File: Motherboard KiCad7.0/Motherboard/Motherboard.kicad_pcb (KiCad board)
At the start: 2 copper layers, 83.8 x 83.8 mm, 92 parts, among them J1 USB_B_Micro, J10 430450200, J11 430450200, J12 430450200, J2 SWD_01x04_Pin, J3 430450200, J4 430450200, J5 B04B-XASK-1, J6 430450200, J7 430450200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

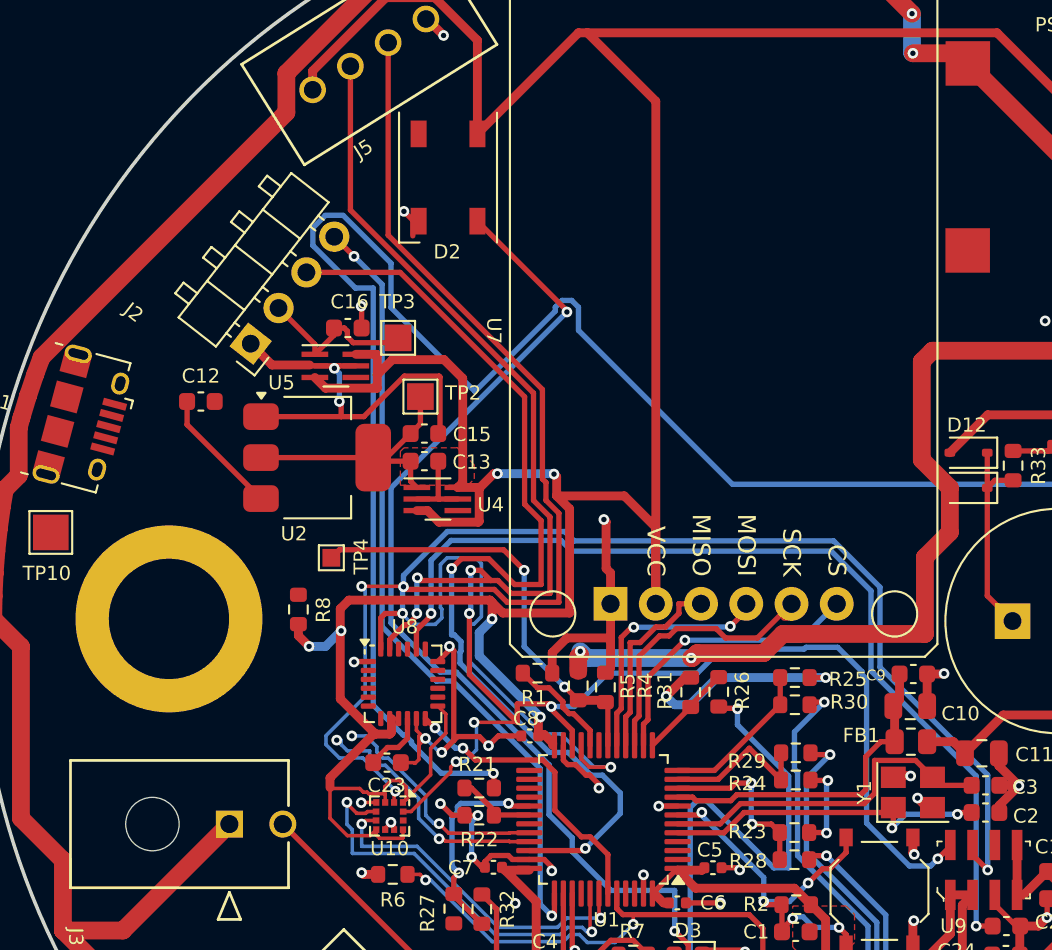
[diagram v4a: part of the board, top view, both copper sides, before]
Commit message: Ran USB differential pair
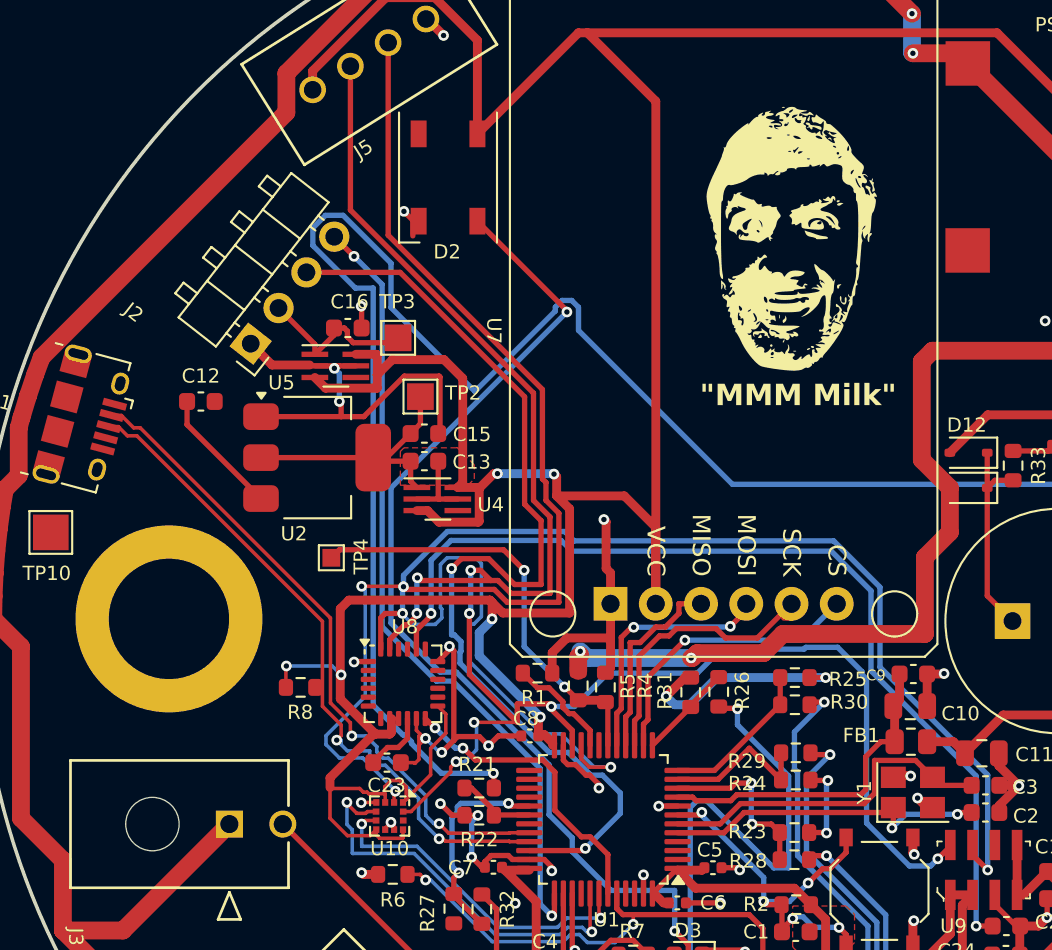
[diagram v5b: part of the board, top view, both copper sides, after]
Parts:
- moved R8 4.38 mm to (168.2, 126.8), turned to 180 degrees
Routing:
- net USB_D-: track 13.1 -> 37.2 mm
- net USB_D+: track 14.1 -> 37.8 mm
- net +3.3V: track 377.8 -> 378.6 mm
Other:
- board text added: "{dblquote}MMM Milk{dblquote}"

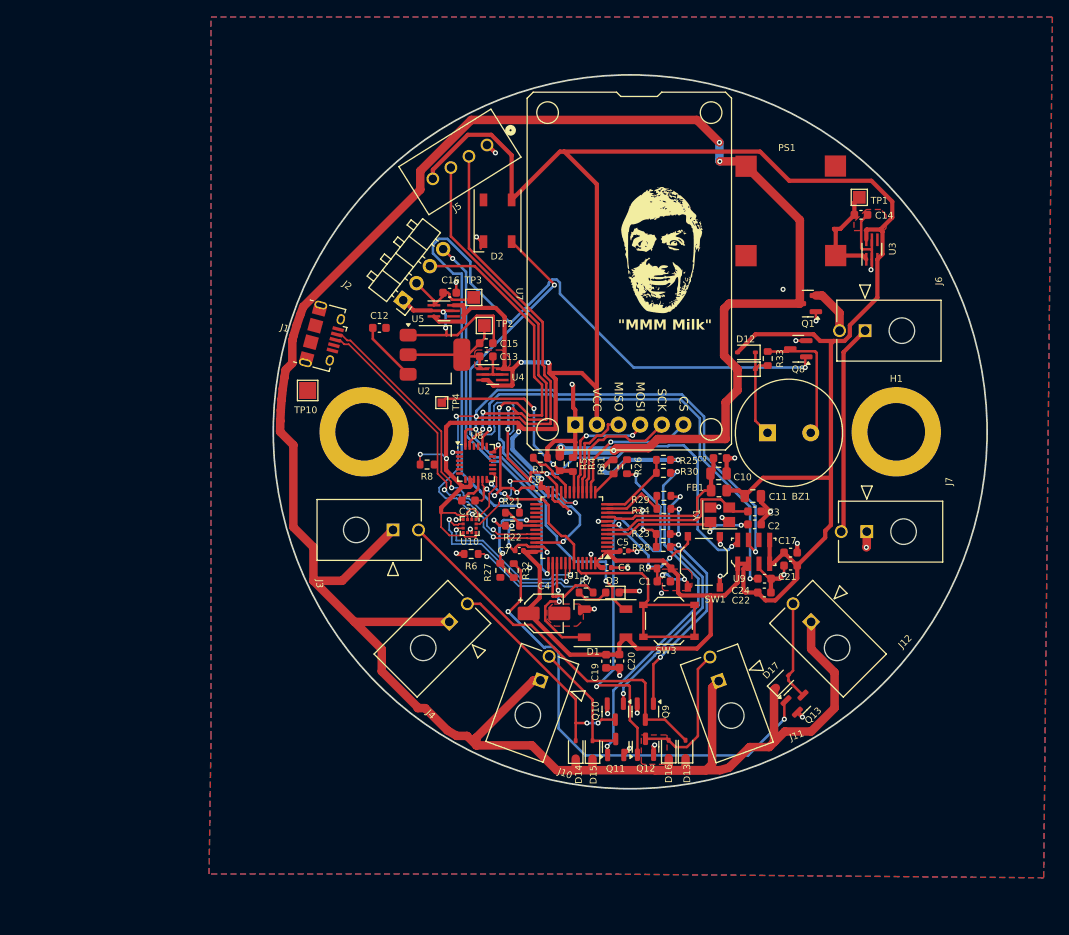
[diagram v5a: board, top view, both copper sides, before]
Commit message: Minor fixes
Added rev. number, list of contributors to layout. Added part numbers to some components in schematic. Generated BOMs using Kennan's plugin
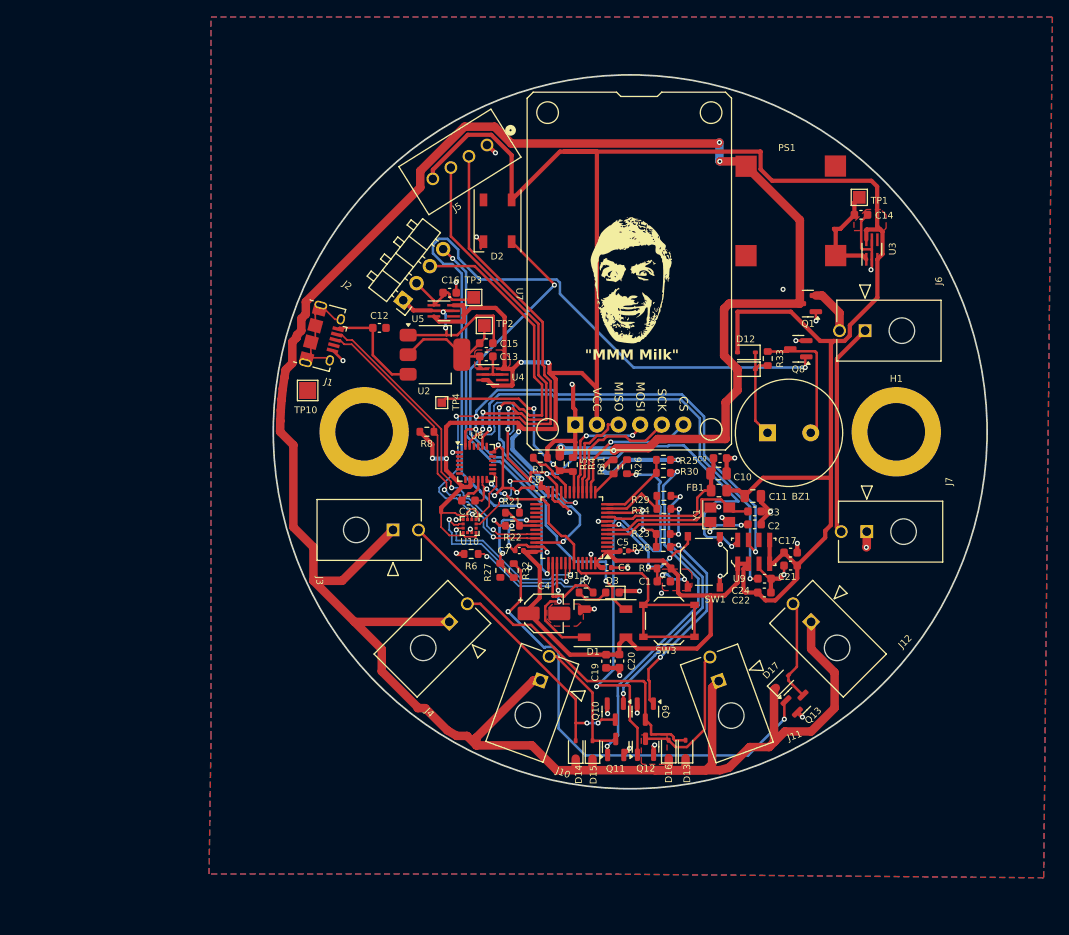
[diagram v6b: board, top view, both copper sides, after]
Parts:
- moved R8 3.85 mm to (168.2, 122.9)
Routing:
- net unconnected-(J1-Shield-Pad6): track 0.00 -> 12.1 mm
- net +3.3V: track 378.6 -> 386.8 mm
- net /USB_5V: track 7.56 -> 12.8 mm
- net Net-(Q8-G): track 96.1 -> 90.9 mm
- net SCL: track 107.5 -> 111.8 mm
- net GND: track 150.1 -> 152.1 mm, vias 50 -> 51
- net V_REGUSB: track 15.1 -> 16.6 mm
- net Net-(Q12-G): track 51.0 -> 52.4 mm
- net Net-(D13-A): track 44.2 -> 44.9 mm
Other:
- board text added: "Rev. 1.0 Contributors: Kennan Bays Joachim Blohm Mohamad Gapre"

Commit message: Additional changes
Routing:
- net GND: track 152.1 -> 150.7 mm
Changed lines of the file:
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@@
   (segment (start 187.45 138.325) (end 187.45 137.273685) (width 0.3) (layer "F.Cu") (net 4))
   (segment (start 184.948675 132.198675) (end 184.430417 131.680417) (width 0.3) (layer "F.Cu") (net 4))
-  (segment (start 186.15 144.225) (end 186.65 143.725) (width 0.5) (layer "F.Cu") (net 4))
   (segment (start 202.575 139.9) (end 202.625 139.85) (width 0.5) (layer "F.Cu") (net 4))
   (segment (start 176.8 129.72353) (end 177.1 129.42353) (width 0.3) (layer "F.Cu") (net 4))
-  (segment (start 185.35 120.075) (end 185.6 120.325) (width 0.5) (layer "F.Cu") (net 4))
   (segment (start 181.87812 136.4125) (end 181.0375 136.4125) (width 0.3) (layer "F.Cu") (net 4))
   (segment (start 220.425 103.775) (end 220.325 103.875) (width 0.3) (layer "F.Cu") (net 4))
@@
   (segment (start 210.1125 139.6625) (end 210.1 139.675) (width 0.3) (layer "F.Cu") (net 4))
   (segment (start 165.9 111.475) (end 165.975 111.55) (width 0.5) (layer "F.Cu") (net 4))
-  (segment (start 185.35 117.45) (end 185.225 117.325) (width 0.5) (layer "F.Cu") (net 4))
   (segment (start 194.8 160.825) (end 194.8 159.8) (width 0.5) (layer "F.Cu") (net 4))
   (segment (start 194.8 159.8) (end 194.925 159.675) (width 0.5) (layer "F.Cu") (net 4))
@@
   (segment (start 219.175 98.175) (end 219.925 97.425) (width 0.3) (layer "F.Cu") (net 4))
   (segment (start 169 108.7) (end 170.375 108.7) (width 0.3) (layer "F.Cu") (net 4))
-  (segment (start 185.6 120.325) (end 185.6 122.059) (width 0.5) (layer "F.Cu") (net 4))
   (segment (start 202.575 135.175) (end 202.575 136.05) (width 0.5) (layer "F.Cu") (net 4))
   (segment (start 185.45 123.975) (end 183.15 123.975) (width 0.5) (layer "F.Cu") (net 4))
@@
   (segment (start 158.325 114.55) (end 157.140889 113.365889) (width 0.3) (layer "F.Cu") (net 4))
   (segment (start 207.4 131.15) (end 208.525 132.275) (width 0.5) (layer "F.Cu") (net 4))
+  (segment (start 185.6 117.875) (end 185.6 122.059) (width 0.5) (layer "F.Cu") (net 4))
   (segment (start 179.865 136.19) (end 180.0875 136.4125) (width 0.3) (layer "F.Cu") (net 4))
   (segment (start 182.95 130.84062) (end 182.95 130) (width 0.3) (layer "F.Cu") (net 4))
   (segment (start 187.45 137.273685) (end 187.450255 137.27343) (width 0.3) (layer "F.Cu") (net 4))
-  (segment (start 185.35 120.075) (end 185.35 117.45) (width 0.5) (layer "F.Cu") (net 4))
   (segment (start 182.3 137.05) (end 182.3 136.83438) (width 0.3) (layer "F.Cu") (net 4))
   (segment (start 173.272498 134.32394) (end 173.4475 134.498942) (width 0.2) (layer "F.Cu") (net 4))
@@
   (via (at 176.05 133.275) (size 0.6) (drill 0.3) (layers "F.Cu" "B.Cu") (net 4))
   (via (at 202.625 139.85) (size 0.6) (drill 0.3) (layers "F.Cu" "B.Cu") (net 4))
-  (via (at 185.225 117.325) (size 0.6) (drill 0.3) (layers "F.Cu" "B.Cu") (net 4))
+  (via (at 185.6 117.875) (size 0.6) (drill 0.3) (layers "F.Cu" "B.Cu") (net 4))
   (segment (start 189.2 127.725) (end 190.05 127.725) (width 0.5) (layer "B.Cu") (net 4))
   (segment (start 197.725 134.925) (end 197.725 132.05) (width 0.3) (layer "B.Cu") (net 4))

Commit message: Added board name and logo
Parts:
- added G***: LOGO, LOGO, B.Cu at (191.1, 106.7)
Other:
- board text added: "Prometheus Rev. 1.0 Contributors: Kennan Bays Joachim Blohm Mohamad Gapre"
- board text removed: "Rev. 1.0 Contributors: Kennan Bays Joachim Blohm Mohamad Gapre"
